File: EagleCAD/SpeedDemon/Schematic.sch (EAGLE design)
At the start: 2 parts, among them U1 LM3676

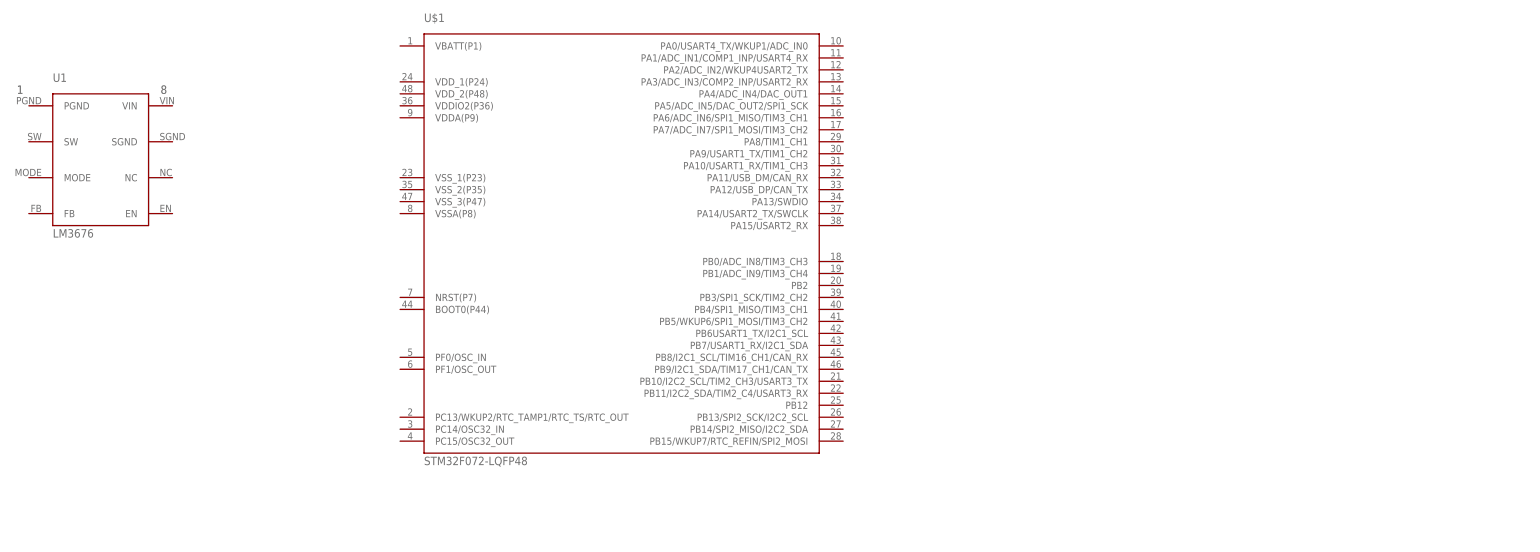
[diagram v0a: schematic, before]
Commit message: Zach I modified the schematic and added the Serial Wire Debug (SWD) connections based off Linyi's document. Let me know what you think. We should double check this together.
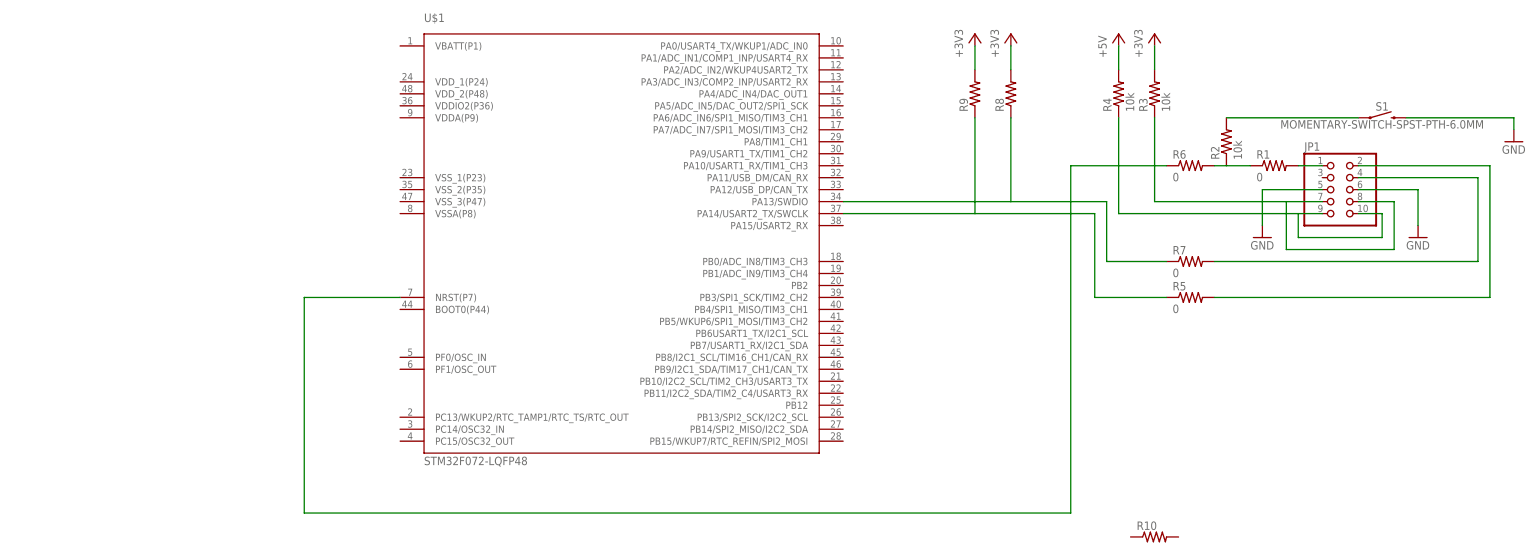
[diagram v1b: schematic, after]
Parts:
- removed U1: LM3676, LM3676:LM3676
- added JP1: (no value), pinhead:PINHD-2X5
- added R1, R5, R6, R7: 0, rcl:R-US_R0805
- added R10, R8, R9: (no value), rcl:R-US_R0805
- added R2, R3, R4: 10k, rcl:R-US_R0805
- added S1: MOMENTARY-SWITCH-SPST-PTH-6.0MM, SparkFun-Switches:MOMENTARY-SWITCH-SPST-PTH-6.0MM
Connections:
- new net +3V3: R3.2, R8.2, R9.2
- new net +5V: R4.2
- new net GND: JP1.5, JP1.6, S1.2
- new net N$1: R6.1, U$1.NRST(P7)
- new net N$10: R7.1, R8.1, U$1.PA13/SWDIO
- new net N$2: JP1.1, R1.2
- new net N$3: JP1.10, JP1.9, R4.1
- new net N$4: R2.2, S1.1
- new net N$5: JP1.2, R5.2
- new net N$6: JP1.7, JP1.8, R3.1
- new net N$7: R5.1, R9.1, U$1.PA14/USART2_TX/SWCLK
- new net N$8: R1.1, R2.1, R6.2
- new net N$9: JP1.4, R7.2

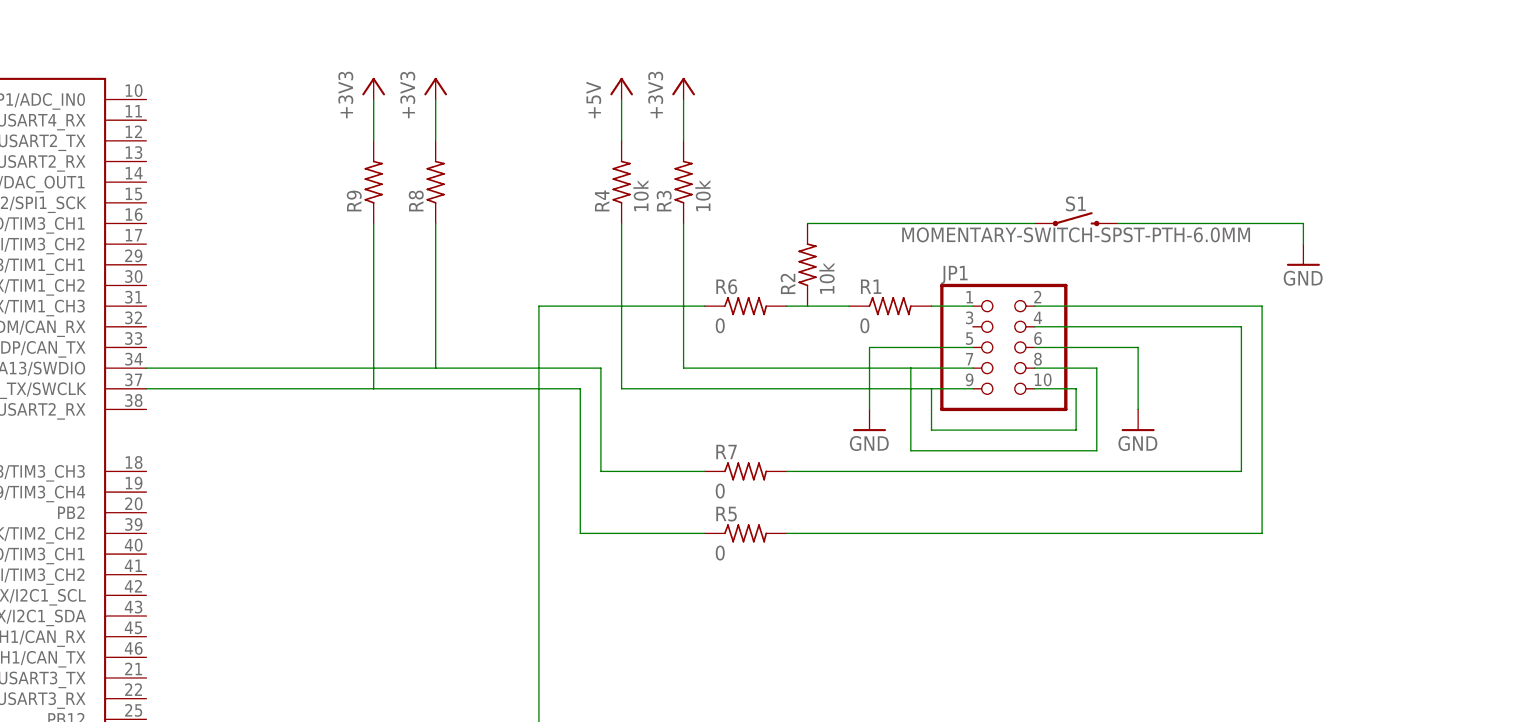
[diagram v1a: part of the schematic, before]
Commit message: Zach checkout the schematic. I added the SWD connections. We should review this together.
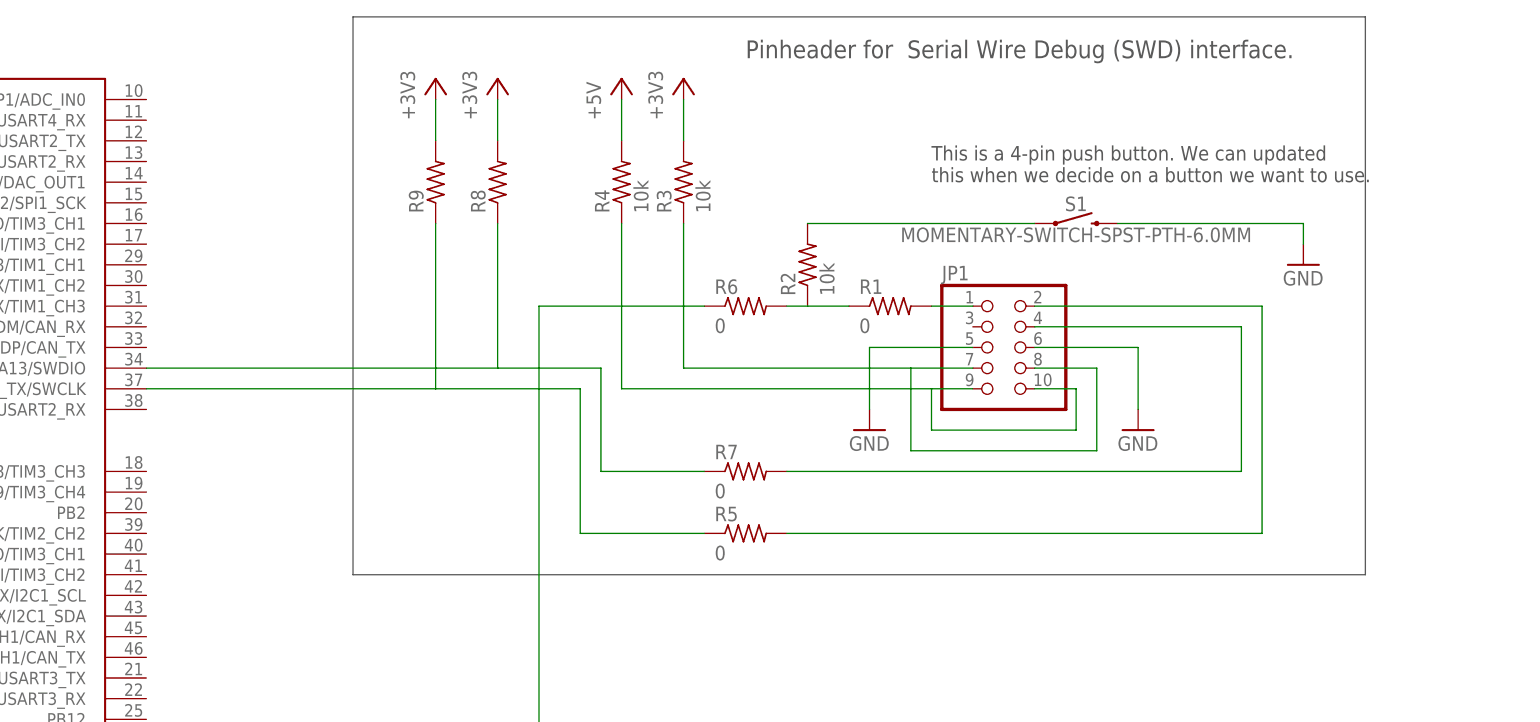
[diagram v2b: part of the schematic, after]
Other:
- note added: "Pinheader for Serial Wire Debug (SWD) interface."
- note added: "This is a 4-pin push button. We can updated this when we decide on a button we want to use."
- moved on the sheet: R8, R9
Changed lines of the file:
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@@
 <sheet>
 <plain>
+<wire x1="256.54" y1="190.5" x2="256.54" y2="121.92" width="0.1524" layer="97"/>
+<wire x1="256.54" y1="121.92" x2="381" y2="121.92" width="0.1524" layer="97"/>
+<wire x1="381" y1="121.92" x2="381" y2="190.5" width="0.1524" layer="97"/>
+<wire x1="381" y1="190.5" x2="256.54" y2="190.5" width="0.1524" layer="97"/>
+<text x="304.8" y="185.42" size="2.1844" layer="97">Pinheader for  Serial Wire Debug (SWD) interface.</text>
+<text x="327.66" y="170.18" size="1.778" layer="97">This is a 4-pin push button. We can updated
+this when we decide on a button we want to use.</text>
 </plain>
 <instances>
@@
 <instance part="R6" gate="G$1" x="304.8" y="154.94"/>
 <instance part="R7" gate="G$1" x="304.8" y="134.62"/>
-<instance part="R8" gate="G$1" x="266.7" y="170.18" rot="R90"/>
-<instance part="R9" gate="G$1" x="259.08" y="170.18" rot="R90"/>
+<instance part="R8" gate="G$1" x="274.32" y="170.18" rot="R90"/>
+<instance part="R9" gate="G$1" x="266.7" y="170.18" rot="R90"/>
 <instance part="R10" gate="G$1" x="297.18" y="76.2"/>
 <instance part="S1" gate="G$1" x="345.44" y="165.1"/>
@@
 <instance part="GND2" gate="1" x="353.06" y="139.7"/>
 <instance part="GND3" gate="1" x="320.04" y="139.7"/>
-<instance part="+3V2" gate="G$1" x="266.7" y="182.88"/>
-<instance part="+3V3" gate="G$1" x="259.08" y="182.88"/>
+<instance part="+3V2" gate="G$1" x="274.32" y="182.88"/>
+<instance part="+3V3" gate="G$1" x="266.7" y="182.88"/>
 </instances>
 <busses>
@@
 <pinref part="+3V3" gate="G$1" pin="+3V3"/>
 <pinref part="R9" gate="G$1" pin="2"/>
-<wire x1="259.08" y1="180.34" x2="259.08" y2="175.26" width="0.1524" layer="91"/>
+<wire x1="266.7" y1="180.34" x2="266.7" y2="175.26" width="0.1524" layer="91"/>
 </segment>
 <segment>
 <pinref part="R8" gate="G$1" pin="2"/>
 <pinref part="+3V2" gate="G$1" pin="+3V3"/>
-<wire x1="266.7" y1="175.26" x2="266.7" y2="180.34" width="0.1524" layer="91"/>
+<wire x1="274.32" y1="175.26" x2="274.32" y2="180.34" width="0.1524" layer="91"/>
 </segment>
 </net>
@@
 <wire x1="284.48" y1="127" x2="284.48" y2="144.78" width="0.1524" layer="91"/>
 <pinref part="U$1" gate="G$1" pin="PA14/USART2_TX/SWCLK"/>
-<wire x1="284.48" y1="144.78" x2="259.08" y2="144.78" width="0.1524" layer="91"/>
+<wire x1="284.48" y1="144.78" x2="266.7" y2="144.78" width="0.1524" layer="91"/>
 <pinref part="R5" gate="G$1" pin="1"/>
 <pinref part="R9" gate="G$1" pin="1"/>
-<wire x1="259.08" y1="144.78" x2="231.14" y2="144.78" width="0.1524" layer="91"/>
-<wire x1="259.08" y1="165.1" x2="259.08" y2="144.78" width="0.1524" layer="91"/>
+<wire x1="266.7" y1="144.78" x2="231.14" y2="144.78" width="0.1524" layer="91"/>
+<wire x1="266.7" y1="165.1" x2="266.7" y2="144.78" width="0.1524" layer="91"/>
 </segment>
 </net>
@@
 <wire x1="287.02" y1="134.62" x2="287.02" y2="147.32" width="0.1524" layer="91"/>
 <pinref part="U$1" gate="G$1" pin="PA13/SWDIO"/>
-<wire x1="287.02" y1="147.32" x2="266.7" y2="147.32" width="0.1524" layer="91"/>
+<wire x1="287.02" y1="147.32" x2="274.32" y2="147.32" width="0.1524" layer="91"/>
 <pinref part="R7" gate="G$1" pin="1"/>
 <pinref part="R8" gate="G$1" pin="1"/>
-<wire x1="266.7" y1="147.32" x2="231.14" y2="147.32" width="0.1524" layer="91"/>
-<wire x1="266.7" y1="165.1" x2="266.7" y2="147.32" width="0.1524" layer="91"/>
+<wire x1="274.32" y1="147.32" x2="231.14" y2="147.32" width="0.1524" layer="91"/>
+<wire x1="274.32" y1="165.1" x2="274.32" y2="147.32" width="0.1524" layer="91"/>
 </segment>
 </net>
@@
 </drawing>
 <compatibility>
+<note version="6.3" minversion="6.2.2" severity="warning">
+Since Version 6.2.2 text objects can contain more than one line,
+which will not be processed correctly with this version.
+</note>
 <note version="8.2" severity="warning">
 Since Version 8.2, EAGLE supports online libraries. The ids

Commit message: added partial power circuit to schematic, added 0805_generics.lbr (generic 0805 SMD RCL parts) to EagleCAD folder
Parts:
- added BT1: (no value), SparkFun-Batteries:BATTERY-9V
- added C1: 4.7uF, 0805_generics:C_0805_NP
- added C2: 10uF, 0805_generics:C_0805_NP
- added L1: 2.2uH, 0805_generics:L_0805
- added U1: LM3676, LM3676:LM3676
- R5, R7: value 0 -> 22
- R8, R9: value (none) -> 10k
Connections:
- net N$1 renamed FL_RESET
- net N$10 renamed FL_SWDIO
- net N$7 renamed FL_SWCLK
- new net N$1: C1.1, U1.VIN
- new net N$11: L1.2, U1.FB
- new net N$7: U1.EN
- net +3V3: now also C2.1, L1.1, U1.SW
- net GND: now also BT1.-, C1.2, C2.2, U1.MODE, U1.PGND, U1.SGND
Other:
- note added: "Power supply/reg"
- note added: "This is a 4-pin push button. We can update this when we decide on a button we want to use."
- note added: "this is a generic battery"
- note added: "timing/FF circuit goes here!"
- note removed: "This is a 4-pin push button. We can updated this when we decide on a button we want to use."
- moved on the sheet: JP1, R1, R2, R3, R4, R5, R6, R7, R8, R9, S1

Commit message: Added power switch logic to schematic (mostly done). Added related parts to new library.
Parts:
- removed U$1: STM32F072-LQFP48, stm32f0:STM32F072-LQFP48
- added C3: 100nF, 0805_generics:C_0805_NP
- added C4: 1uF, 0805_generics:C_0805_NP
- added C5: 4.7uF, 0805_generics:C_0805_NP
- added D1: 1N4148DO35-7, diode:1N4148DO35-7
- added Q1: DMC2700, DMC2700:DMC2700_SOT-23-6
- added R11: 100k, 0805_generics:R_0805
- added R12: 10k, 0805_generics:R_0805
- added R13: 330k, 0805_generics:R_0805
- added R14: 270k, 0805_generics:R_0805
- added S2: MOMENTARY-SWITCH-SPST-PTH-6.0MM, SparkFun-Switches:MOMENTARY-SWITCH-SPST-PTH-6.0MM
- added U3: STM32F072-LQFP48, stm32f0:STM32F072-LQFP48
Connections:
- removed net N$7: U1.EN
- new net FF_OUTPUT: C5.1, Q1.D2, R14.2, U1.EN
- new net N$10: L1.1, U1.FB
- new net N$15: D1.A, R13.1, R14.1
- new net Q1_D1: C3.2, C4.2, Q1.D1, Q1.G2, R11.1
- new net VBATT_RAW: BT1.+, C1.1, C3.1, Q1.S2, R11.2, R12.2, U1.VIN
- net +3V3: now also L1.2; no longer L1.1
- net FL_RESET: now also U3.NRST(P7); no longer U$1.NRST(P7)
- net FL_SWCLK: now also U3.PA14/USART2_TX/SWCLK; no longer U$1.PA14/USART2_TX/SWCLK
- net FL_SWDIO: now also U3.PA13/SWDIO; no longer U$1.PA13/SWDIO
- net GND: now also Q1.S1, S2.2
- net N$1: now also C5.2, Q1.G1, R13.2; no longer C1.1, U1.VIN
- net N$11: now also C4.1, D1.C, R12.1, S2.1; no longer L1.2, U1.FB
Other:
- note added: "*BT1 is a generic battery--we may need to add charging circuitry"
- note added: "Power Switch Logic"
- note added: "find equivalent diode in SMD pkg"
- note added: "pwr/mode_SW (should be DPST)"
- note removed: "this is a generic battery"
- note removed: "timing/FF circuit goes here!"
- moved on the sheet: BT1, C1, C2, L1, U1

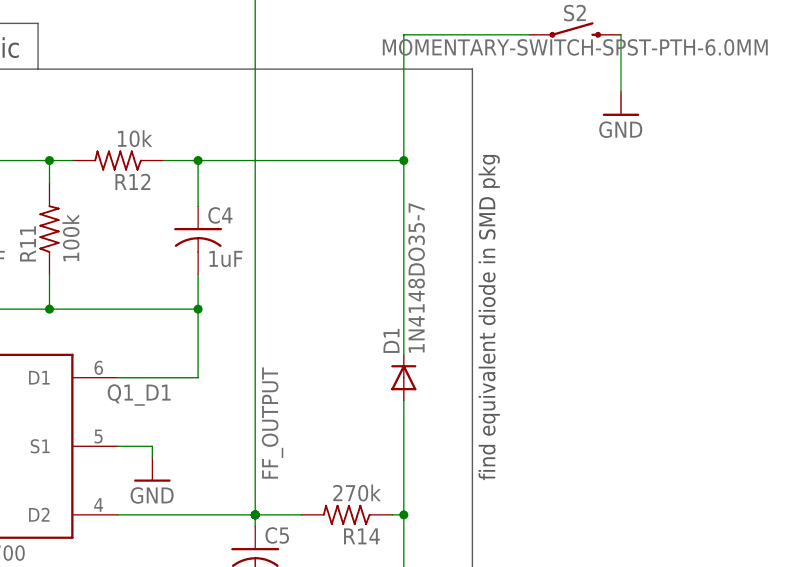
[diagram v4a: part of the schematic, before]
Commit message: Added 1n4148 SMD package to library and to power button schematic
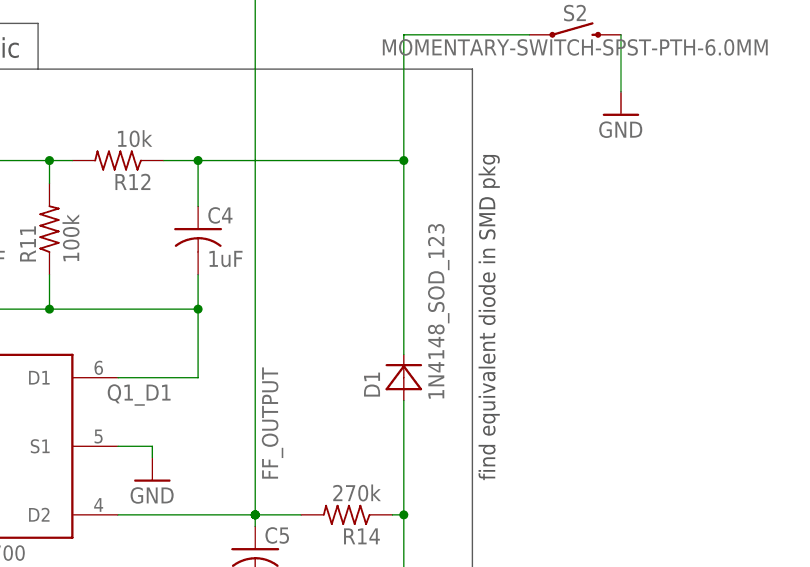
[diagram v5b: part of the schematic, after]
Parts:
- D1: value 1N4148DO35-7 -> 1N4148_SOD_123; device diode:1N4148DO35-7 -> LCRD_SMD_generics:1N4148_SOD_123
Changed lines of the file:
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@@
 <part name="R14" library="0805_generics" deviceset="R_0805" device="" value="270k"/>
 <part name="GND8" library="supply1" library_urn="urn:adsk.eagle:library:371" deviceset="GND" device=""/>
-<part name="D1" library="diode" library_urn="urn:adsk.eagle:library:210" deviceset="1N4148" device="DO35-7" package3d_urn="urn:adsk.eagle:package:43339/1"/>
+<part name="D1" library="LCRD_SMD_generics" deviceset="1N4148_SOD_123" device=""/>
 </parts>
 <sheets>
@@
 <instance part="R14" gate="G$1" x="77.47" y="102.87" rot="R180"/>
 <instance part="GND8" gate="1" x="107.95" y="147.32"/>
-<instance part="D1" gate="G$1" x="83.82" y="118.11" rot="R90"/>
+<instance part="D1" gate="&gt;NAME" x="83.82" y="118.11" rot="R90"/>
 </instances>
 <busses>
@@
 <wire x1="60.96" y1="137.16" x2="60.96" y2="142.24" width="0.1524" layer="91"/>
 <junction x="60.96" y="142.24"/>
-<pinref part="D1" gate="G$1" pin="C"/>
+<pinref part="D1" gate="&gt;NAME" pin="C"/>
 </segment>
 </net>
@@
 <wire x1="83.82" y1="92.71" x2="83.82" y2="102.87" width="0.1524" layer="91"/>
 <wire x1="83.82" y1="102.87" x2="82.55" y2="102.87" width="0.1524" layer="91"/>
-<pinref part="D1" gate="G$1" pin="A"/>
 <wire x1="83.82" y1="102.87" x2="83.82" y2="115.57" width="0.1524" layer="91"/>
 <junction x="83.82" y="102.87"/>
-</segment>
-</net>
+<pinref part="D1" gate="&gt;NAME" pin="A"/>
+</segment>
+</net>

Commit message: More added to schem, incl. power scheme for MCU and seonsor input section. NOTE: Working SMD passives library has been renamed LCRD_SMD_generics.lbr
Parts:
- added C10, C6, C8, C9: 100nF, 0805_generics:C_0805_NP
- added C11: 10nF, 0805_generics:C_0805_NP
- added C12, C13: 4.7uF, 0805_generics:C_0805_NP
- added C14: 1uF, 0805_generics:C_0805_NP
- added C7: 4.7nF, 0805_generics:C_0805_NP
- added H1: TO_PIN_1, holes:MOUNT-PAD-SQUARE2.8
- added H2: TO_PIN_2, holes:MOUNT-PAD-SQUARE2.8
- added H3: TO_PIN_3, holes:MOUNT-PAD-SQUARE2.8
- added H4: BATT+, holes:MOUNT-HOLE4.1
- added H5: BATT-, holes:MOUNT-HOLE4.1
- added R15: 10k, 0805_generics:R_0805
- added R16: 1.5M, 0805_generics:R_0805
- added R17: 2.2M, 0805_generics:R_0805
- S2: value MOMENTARY-SWITCH-SPST-PTH-6.0MM -> button-SPST
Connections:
- removed net VBATT_RAW: BT1.+, C1.1, C3.1, Q1.S2, R11.2, R12.2, U1.VIN
- new net N$7: R16.1, R17.2, U3.VBATT(P1)
- new net SENSOR_SIG_OP: C7.1, H2.MOUNT, R15.2
- new net V+: BT1.+, C1.1, C3.1, C6.1, H3.MOUNT, Q1.S2, R11.2, R12.2, R15.1, R16.2, U1.VIN
- net +3V3: now also C10.1, C11.1, C12.1, C13.1, C14.1, C8.1, C9.1, U3.VDDA(P9), U3.VDDIO2(P36), U3.VDD_1(P24), U3.VDD_2(P48)
- net GND: now also C10.2, C11.2, C12.2, C13.2, C14.2, C6.2, C7.2, C8.2, C9.2, H1.MOUNT, R17.1, U3.VSSA(P8), U3.VSS_1(P23), U3.VSS_2(P35), U3.VSS_3(P47)
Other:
- note added: "(See datasheet 'en.DM00091510.pdf' p. 60/128 for more info)"
- note added: "(should be DPST)"
- note added: "Aim for ~2.0uA @ min 1.65 max 3.6V. These should work well"
- note added: "FROM SENSOR MODULE CONN"
- note added: "MCU Power Filtering"
- note added: "May have to change resistor vals depending on battery used."
- note added: "Place components on underside of board as close as poss."
- note added: "p. 49/128 for more info)"
- note added: "pwr/mode_SW"
- note added: "to corresponding pins (see datasheet 'en.DM00090510.pdf'"
- note added: "with max 6.1V from the battery across all charge ranges."
- note removed: "pwr/mode_SW (should be DPST)"
- moved on the sheet: BT1, C1, C2, C3, C4, C5, D1, JP1, L1, Q1, R1, R11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
